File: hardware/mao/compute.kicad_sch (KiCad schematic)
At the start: 46 parts, among them J201 TAG, U201 ESP32-S3-WROOM-1-N8R2, U202 TCA6408ARGTR

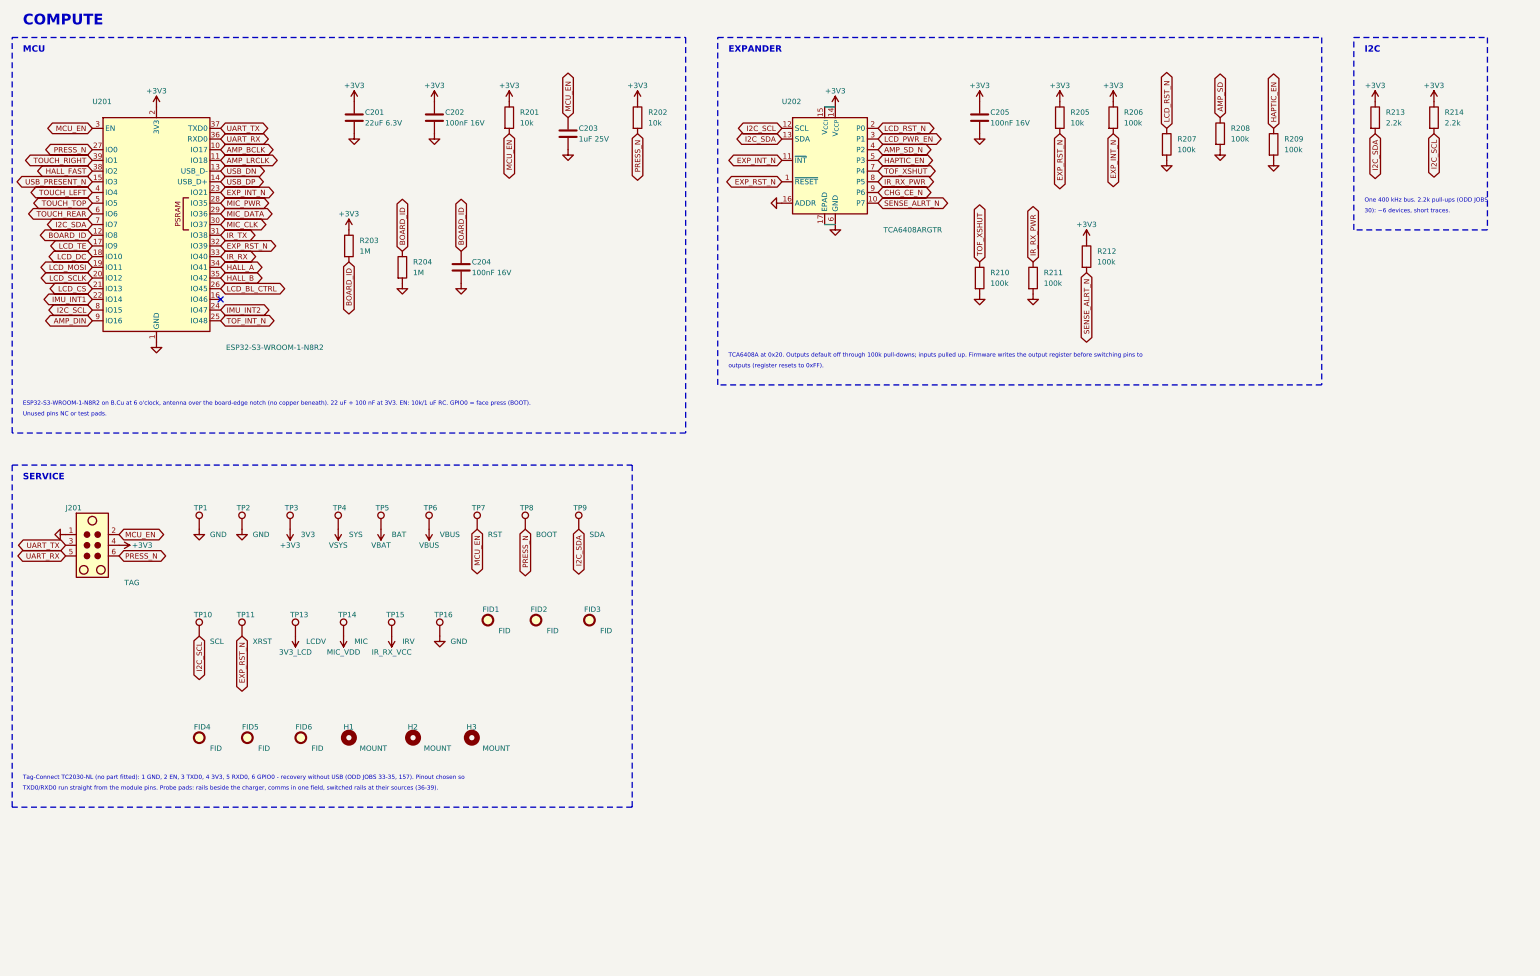
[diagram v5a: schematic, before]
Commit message: A1 capture: Gate C architecture on the A0 puck (schematic, ERC 0)
circuit.py now describes MAO_MAIN A1 (ERC 0 at all severities, 137 parts, 75 nets):
- ESP32-S3-MINI-1-N8 on RF_Module:ESP32-S2-MINI-1 (Gate C land audit); GPIO0 = BOOT pad only
  (10k + TP8), GPIO3/45/46 NC, 22R + DNP 10 pF on USB at the module, VBUS_SENSE 100k/150k.
- BQ25185 (ILIM/VSET 18k: 4.2 V / 500 mA; ISET 1.43k: 210 mA as A0; TS/MR to the NTC, DNP 10k,
  TSMR pad; /CE 100k pull-down; STAT1/2 10k to +3V3) replaces BQ24073.
- TPS62840 (VSET 102k = 3.2 V, SLVSEC6D table 1; 2.2 uH, CIN 4.7 uF, COUT 10 uF; MODE/STOP low,
  EN to VIN) replaces TPS63802 and its UVLO/FB dividers; LINK_REG 0R added, LINK_BAT kept.
- ICM-42670-P replaces LSM6DSOX on the same land (0x68, INT1 100k pull-up, INT2 not wired).
- DRV2605L VDD and pin 6 on +3V3; constant-current backlight sink (TLV9061 + DMG2302UK, 3.3R)
  replaces the AW9364; TPS22916C for the panel rail and the IR receiver rail.
- MAX98357A SD_MODE straight from GPIO9 (2.2k series dropped: +3V3 <= VSYS by topology).
- Removed: touch (4 zones, electrodes, springs), SPH0641, OPT3004, TCA6408A, board-ID divider.
- I2C pull-ups 4.7k; new fixture pads BL, AMP, TE, PRS, HLA, TSMR, CE, IO21, IO26.
- Battery connector stays JST SH: the Gate C JST PH side entry is 4.8 mm tall (KiCad STEP of the
  PH side-entry housing) against the 3.2 mm B-side zone over the cell; owner decision.
Parts kept from A0 keep their references; removed numbers are retired.
New footprint MAO:TI_DLC0008B_VSON-HR-8 (TI land example 4224310/A, from the Gate C generator);
A0-only custom footprints removed. Board name MAO_MAIN_A1; A0 board/outputs removed from this tree
(they stay on the A0 branch).

Co-Authored-By: Claude Opus 5.5 <noreply@anthropic.com>
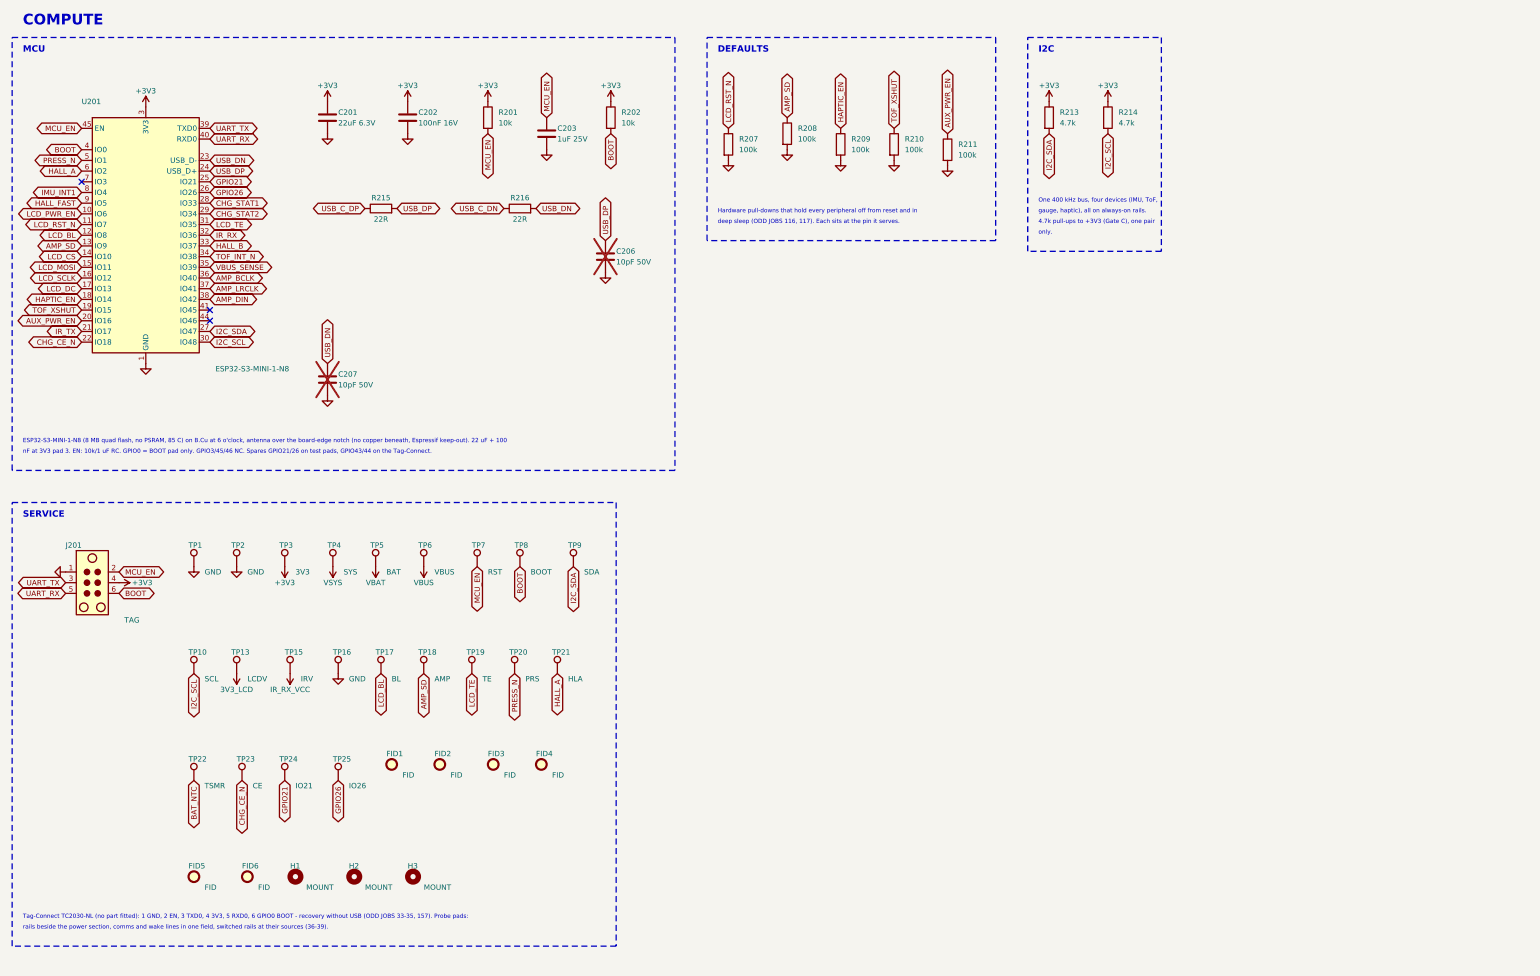
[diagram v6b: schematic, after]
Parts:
- removed C204, C205: 100nF 16V, Capacitor_SMD:C_0402_1005Metric, symbol Device:C
- removed R203, R204: 1M, Resistor_SMD:R_0402_1005Metric, symbol Device:R
- removed R205: 10k, Resistor_SMD:R_0402_1005Metric, symbol Device:R
- removed R206, R212: 100k, Resistor_SMD:R_0402_1005Metric, symbol Device:R
- removed TP11: XRST, TestPoint:TestPoint_Pad_D1.0mm, symbol Connector:TestPoint
- removed TP14: MIC, TestPoint:TestPoint_Pad_D1.0mm, symbol Connector:TestPoint
- removed U202: TCA6408ARGTR, Package_DFN_QFN:VQFN-16-1EP_3x3mm_P0.5mm_EP1.45x1.45mm_ThermalVias, symbol Interface_Expansion:TCA6408ARGT
- added C206, C207: 10pF 50V, Capacitor_SMD:C_0402_1005Metric, symbol Device:C
- added R215, R216: 22R, Resistor_SMD:R_0402_1005Metric, symbol Device:R
- added TP17: BL, TestPoint:TestPoint_Pad_D1.0mm, symbol Connector:TestPoint
- added TP18: AMP, TestPoint:TestPoint_Pad_D1.0mm, symbol Connector:TestPoint
- added TP19: TE, TestPoint:TestPoint_Pad_D1.0mm, symbol Connector:TestPoint
- added TP20: PRS, TestPoint:TestPoint_Pad_D1.0mm, symbol Connector:TestPoint
- added TP21: HLA, TestPoint:TestPoint_Pad_D1.0mm, symbol Connector:TestPoint
- added TP22: TSMR, TestPoint:TestPoint_Pad_D1.0mm, symbol Connector:TestPoint
- added TP23: CE, TestPoint:TestPoint_Pad_D1.0mm, symbol Connector:TestPoint
- added TP24: IO21, TestPoint:TestPoint_Pad_D1.0mm, symbol Connector:TestPoint
- added TP25: IO26, TestPoint:TestPoint_Pad_D1.0mm, symbol Connector:TestPoint
- R213, R214: value 2.2k -> 4.7k; LCSC C25879 -> C25900; MPN 0402WGF2201TCE -> 0402WGF4701TCE
- U201: value ESP32-S3-WROOM-1-N8R2 -> ESP32-S3-MINI-1-N8; footprint RF_Module:ESP32-S3-WROOM-1 -> RF_Module:ESP32-S2-MINI-1; symbol RF_Module:ESP32-S3-WROOM-1 -> RF_Module:ESP32-S3-MINI-1; LCSC C2913204 -> C2913206; MPN ESP32-S3-WROOM-1-N8R2 -> ESP32-S3-MINI-1-N8
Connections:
- net EXP_INT_N is gone; now on net USB_DN: U201.23 (USB_D-)
- net EXP_RST_N is gone; now on net IR_RX: U201.32 (IO36)
- net IMU_INT2 is gone; now on net USB_DP: U201.24 (USB_D+)
- net MIC_CLK is gone; now on net I2C_SCL: U201.30 (IO48)
- net TOUCH_REAR is gone; now on net HALL_A: U201.6 (IO2)
- net TOUCH_RIGHT is gone; now on net UART_TX: U201.39 (TXD0)
- net TOUCH_TOP is gone; now on net PRESS_N: U201.5 (IO1)
- net USB_PRESENT_N is gone; now on net LCD_MOSI: U201.15 (IO11)
- net +3V3: now also U201.3 (3V3); no longer U201.2 (3V3)
- net AMP_BCLK: now also U201.36 (IO40); no longer U201.10 (IO17)
- net AMP_DIN: now also U201.38 (IO42); no longer U201.9 (IO16)
- net AMP_LRCLK: now also U201.37 (IO41); no longer U201.11 (IO18)
- net AMP_SD: now also U201.13 (IO9), TP18.1
- net CHG_CE_N: now also U201.22 (IO18), TP23.1
- net GND: now also U201.2 (GND), U201.42 (GND), U201.43 (GND), U201.46 (GND), U201.47 (GND), U201.48 (GND), U201.49 (GND), U201.50 (GND), U201.51 (GND), U201.52 (GND), U201.53 (GND), U201.54 (GND), U201.55 (GND), U201.56 (GND), U201.57 (GND), U201.58 (GND), U201.59 (GND), U201.60 (GND), U201.61 (GND), U201.62 (GND), U201.63 (GND), U201.64 (GND), U201.65 (GND), C206.2, C207.2; no longer U201.40 (GND), U201.41 (GND)
- net HALL_A: now also TP21.1; no longer U201.34 (IO41)
- net HALL_B: now also U201.33 (IO37); no longer U201.35 (IO42)
- net HALL_FAST: now also U201.9 (IO5); no longer U201.38 (IO2)
- net HAPTIC_EN: now also U201.18 (IO14)
- net I2C_SCL: no longer U201.8 (IO15)
- net I2C_SDA: now also U201.27 (IO47); no longer U201.7 (IO7)
- net IMU_INT1: now also U201.8 (IO4); no longer U201.22 (IO14)
- net IR_RX: no longer U201.33 (IO40)
- net IR_TX: now also U201.21 (IO17); no longer U201.31 (IO38)
- net LCD_CS: now also U201.14 (IO10); no longer U201.21 (IO13)
- net LCD_DC: now also U201.17 (IO13); no longer U201.18 (IO10)
- net LCD_MOSI: no longer U201.19 (IO11)
- net LCD_PWR_EN: now also U201.10 (IO6)
- net LCD_RST_N: now also U201.11 (IO7)
- net LCD_SCLK: now also U201.16 (IO12); no longer U201.20 (IO12)
- net LCD_TE: now also U201.31 (IO35), TP19.1; no longer U201.17 (IO9)
- net MCU_EN: now also U201.45 (EN); no longer U201.3 (EN)
- net PRESS_N: now also TP20.1; no longer J201.6, R202.2, TP8.1, U201.27 (IO0)
- net TOF_INT_N: now also U201.34 (IO38); no longer U201.25 (IO48)
- net TOF_XSHUT: now also U201.19 (IO15)
- net UART_RX: now also U201.40 (RXD0); no longer U201.36 (RXD0)
- net UART_TX: no longer U201.37 (TXD0)
- net USB_DN: now also C207.1, R216.2; no longer U201.13 (USB_D-)
- net USB_DP: now also C206.1, R215.2; no longer U201.14 (USB_D+)
- net BOARD_ID renamed LCD_BL
- net LCD_BL: now also TP17.1
- net IR_RX_PWR renamed AUX_PWR_EN
- net AUX_PWR_EN: now also U201.20 (IO16)
- net LCD_BL_CTRL renamed GPIO26
- net GPIO26: now also TP25.1
- net MIC_DATA renamed CHG_STAT2
- net MIC_PWR renamed CHG_STAT1
- net TOUCH_LEFT renamed BOOT
- net BOOT: now also J201.6, R202.2, TP8.1
- new net BAT_NTC: TP22.1
- new net GPIO21: TP24.1, U201.25 (IO21)
- new net USB_C_DN: R216.1
- new net USB_C_DP: R215.1
- new net VBUS_SENSE: U201.35 (IO39)
- no-connect marks 1 -> 3
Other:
- note added: "4.7k pull-ups to +3V3 (Gate C), one pair"
- note added: "DEFAULTS"
- note added: "ESP32-S3-MINI-1-N8 (8 MB quad flash, no PSRAM, 85 C) on B.Cu at 6 o'clock, antenna over the board-edge notch (no copper beneath, Espressif keep-out). 22 uF + 100"
- note added: "Hardware pull-downs that hold every peripheral off from reset and in"
- note added: "One 400 kHz bus, four devices (IMU, ToF,"
- note added: "Tag-Connect TC2030-NL (no part fitted): 1 GND, 2 EN, 3 TXD0, 4 3V3, 5 RXD0, 6 GPIO0 BOOT - recovery without USB (ODD JOBS 33-35, 157). Probe pads:"
- note added: "deep sleep (ODD JOBS 116, 117). Each sits at the pin it serves."
- note added: "gauge, haptic), all on always-on rails."
- note added: "nF at 3V3 pad 3. EN: 10k/1 uF RC. GPIO0 = BOOT pad only. GPIO3/45/46 NC. Spares GPIO21/26 on test pads, GPIO43/44 on the Tag-Connect."
- note added: "only."
- note added: "rails beside the power section, comms and wake lines in one field, switched rails at their sources (36-39)."
- note removed: "30): ~6 devices, short traces."
- note removed: "ESP32-S3-WROOM-1-N8R2 on B.Cu at 6 o'clock, antenna over the board-edge notch (no copper beneath). 22 uF + 100 nF at 3V3. EN: 10k/1 uF RC. GPIO0 = face press (BOOT)."
- note removed: "EXPANDER"
- note removed: "One 400 kHz bus. 2.2k pull-ups (ODD JOBS"
- note removed: "TCA6408A at 0x20. Outputs default off through 100k pull-downs; inputs pulled up. Firmware writes the output register before switching pins to"
- note removed: "TXD0/RXD0 run straight from the module pins. Probe pads: rails beside the charger, comms in one field, switched rails at their sources (36-39)."
- note removed: "Tag-Connect TC2030-NL (no part fitted): 1 GND, 2 EN, 3 TXD0, 4 3V3, 5 RXD0, 6 GPIO0 - recovery without USB (ODD JOBS 33-35, 157). Pinout chosen so"
- note removed: "Unused pins NC or test pads."
- note removed: "outputs (register resets to 0xFF)."
- title: MAO_MAIN A0 - Compute -> MAO_MAIN A1 - Compute
- moved on the sheet: C201, C202, C203, FID1, FID2, FID3, FID4, FID5, FID6, H1, H2, H3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
